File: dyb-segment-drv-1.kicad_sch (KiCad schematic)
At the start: 33 parts, among them J1 Conn_01x10, SW1 SW_SPDT, U1 AP2112K-1.8

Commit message: schem: add title
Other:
- company: (none) -> Rémi Ait-Younes
- title: (none) -> DYB Segment Driver 1
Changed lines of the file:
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@@
 	(generator_version "10.0")
 	(paper "A4")
+	(title_block
+		(title "DYB Segment Driver 1")
+		(date "2026-09-29")
+		(rev "01")
+		(company "Rémi Ait-Younes")
+	)
 	(rectangle
 		(start 15.24 168.91)

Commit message: schem: reannotate
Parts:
- renumbered C60 to C1, C61 to C2, JP4 to JP1, TP8 to TP1, TP27 to TP17, TP17 to TP18, TP18 to TP19, TP1 to TP2, TP19 to TP20, TP20 to TP21, TP21 to TP22, TP22 to TP23, TP23 to TP24, TP26 to TP25, TP2 to TP3, TP3 to TP4, TP4 to TP5, TP5 to TP6, TP6 to TP7, TP7 to TP8
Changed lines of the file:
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@@
 		(dnp no)
 		(fields_autoplaced yes)
-		(property "Reference" "#PWR0181"
+		(property "Reference" "#PWR07"
 			(at 80.01 191.77 0)
 			(hide yes)
@@
 			(project "dyb-segment-drv-1"
 				(path "/0d1f997b-7d97-47c3-85c1-1ce9346504d0"
-					(reference "#PWR0181")
+					(reference "#PWR07")
 					(unit 1)
 				)
@@
 		(in_pos_files yes)
 		(dnp no)
-		(property "Reference" "TP4"
+		(property "Reference" "TP5"
 			(at 128.778 76.2 0)
 			(show_name no)
@@
 			(project "dyb-segment-drv-1"
 				(path "/0d1f997b-7d97-47c3-85c1-1ce9346504d0"
-					(reference "TP4")
+					(reference "TP5")
 					(unit 1)
 				)
@@
 		(dnp no)
 		(fields_autoplaced yes)
-		(property "Reference" "#PWR0175"
+		(property "Reference" "#PWR03"
 			(at 39.37 198.12 0)
 			(hide yes)
@@
 			(project "dyb-segment-drv-1"
 				(path "/0d1f997b-7d97-47c3-85c1-1ce9346504d0"
-					(reference "#PWR0175")
+					(reference "#PWR03")
 					(unit 1)
 				)
@@
 		(in_pos_files yes)
 		(dnp no)
-		(property "Reference" "#PWR0173"
+		(property "Reference" "#PWR01"
 			(at 20.32 184.15 0)
 			(hide yes)
@@
 			(project "dyb-segment-drv-1"
 				(path "/0d1f997b-7d97-47c3-85c1-1ce9346504d0"
-					(reference "#PWR0173")
+					(reference "#PWR01")
 					(unit 1)
 				)
@@
 		(in_pos_files yes)
 		(dnp no)
-		(property "Reference" "TP6"
+		(property "Reference" "TP7"
 			(at 128.778 81.28 0)
 			(show_name no)
@@
 			(project "dyb-segment-drv-1"
 				(path "/0d1f997b-7d97-47c3-85c1-1ce9346504d0"
-					(reference "TP6")
+					(reference "TP7")
 					(unit 1)
 				)
@@
 		(in_pos_files yes)
 		(dnp no)
-		(property "Reference" "TP8"
+		(property "Reference" "TP1"
 			(at 46.228 175.768 0)
 			(show_name no)
@@
 			(project "dyb-segment-drv-1"
 				(path "/0d1f997b-7d97-47c3-85c1-1ce9346504d0"
-					(reference "TP8")
+					(reference "TP1")
 					(unit 1)
 				)
@@
 		(in_pos_files yes)
 		(dnp no)
-		(property "Reference" "TP23"
+		(property "Reference" "TP24"
 			(at 159.258 110.49 0)
 			(show_name no)
@@
 			(project "dyb-segment-drv-1"
 				(path "/0d1f997b-7d97-47c3-85c1-1ce9346504d0"
-					(reference "TP23")
+					(reference "TP24")
 					(unit 1)
 				)
@@
 		(dnp no)
 		(fields_autoplaced yes)
-		(property "Reference" "#PWR0176"
+		(property "Reference" "#PWR04"
 			(at 50.8 198.12 0)
 			(hide yes)
@@
 			(project "dyb-segment-drv-1"
 				(path "/0d1f997b-7d97-47c3-85c1-1ce9346504d0"
-					(reference "#PWR0176")
+					(reference "#PWR04")
 					(unit 1)
 				)
@@
 		(dnp no)
 		(fields_autoplaced yes)
-		(property "Reference" "#FLG02"
+		(property "Reference" "#FLG01"
 			(at 71.12 191.135 0)
 			(hide yes)
@@
 			(project "dyb-segment-drv-1"
 				(path "/0d1f997b-7d97-47c3-85c1-1ce9346504d0"
-					(reference "#FLG02")
+					(reference "#FLG01")
 					(unit 1)
 				)
@@
 		(in_pos_files yes)
 		(dnp no)
-		(property "Reference" "TP26"
+		(property "Reference" "TP25"
 			(at 159.258 113.03 0)
 			(show_name no)
@@
 			(project "dyb-segment-drv-1"
 				(path "/0d1f997b-7d97-47c3-85c1-1ce9346504d0"
-					(reference "TP26")
+					(reference "TP25")
 					(unit 1)
 				)
@@
 		(in_pos_files yes)
 		(dnp no)
-		(property "Reference" "TP7"
+		(property "Reference" "TP8"
 			(at 128.778 83.82 0)
 			(show_name no)
@@
 			(project "dyb-segment-drv-1"
 				(path "/0d1f997b-7d97-47c3-85c1-1ce9346504d0"
-					(reference "TP7")
+					(reference "TP8")
 					(unit 1)
 				)
@@
 		(dnp no)
 		(fields_autoplaced yes)
-		(property "Reference" "C61"
+		(property "Reference" "C2"
 			(at 54.61 185.4199 0)
 			(show_name no)
@@
 			(project "dyb-segment-drv-1"
 				(path "/0d1f997b-7d97-47c3-85c1-1ce9346504d0"
-					(reference "C61")
+					(reference "C2")
 					(unit 1)
 				)
@@
 		(dnp no)
 		(fields_autoplaced yes)
-		(property "Reference" "#PWR0178"
+		(property "Reference" "#PWR06"
 			(at 76.2 196.85 0)
 			(hide yes)
@@
 			(project "dyb-segment-drv-1"
 				(path "/0d1f997b-7d97-47c3-85c1-1ce9346504d0"
-					(reference "#PWR0178")
+					(reference "#PWR06")
 					(unit 1)
 				)
@@
 		(in_pos_files yes)
 		(dnp no)
-		(property "Reference" "#PWR0180"
+		(property "Reference" "#PWR09"
 			(at 123.19 100.33 0)
 			(hide yes)
@@
 			(project "dyb-segment-drv-1"
 				(path "/0d1f997b-7d97-47c3-85c1-1ce9346504d0"
-					(reference "#PWR0180")
+					(reference "#PWR09")
 					(unit 1)
 				)
@@
 		(in_pos_files yes)
 		(dnp no)
-		(property "Reference" "TP20"
+		(property "Reference" "TP21"
 			(at 159.258 102.87 0)
 			(show_name no)
@@
 			(project "dyb-segment-drv-1"
 				(path "/0d1f997b-7d97-47c3-85c1-1ce9346504d0"
-					(reference "TP20")
+					(reference "TP21")
 					(unit 1)
 				)
@@
 		(in_pos_files yes)
 		(dnp no)
-		(property "Reference" "#PWR0177"
+		(property "Reference" "#PWR05"
 			(at 53.34 184.15 0)
 			(hide yes)
@@
 			(project "dyb-segment-drv-1"
 				(path "/0d1f997b-7d97-47c3-85c1-1ce9346504d0"
-					(reference "#PWR0177")
+					(reference "#PWR05")
 					(unit 1)
 				)
@@
 		(in_pos_files yes)
 		(dnp no)
-		(property "Reference" "TP22"
+		(property "Reference" "TP23"
 			(at 159.258 107.95 0)
 			(show_name no)
@@
 			(project "dyb-segment-drv-1"
 				(path "/0d1f997b-7d97-47c3-85c1-1ce9346504d0"
-					(reference "TP22")
+					(reference "TP23")
 					(unit 1)
 				)
@@
 		(in_pos_files yes)
 		(dnp no)
-		(property "Reference" "TP27"
+		(property "Reference" "TP17"
 			(at 159.258 86.36 0)
 			(show_name no)
@@
 			(project "dyb-segment-drv-1"
 				(path "/0d1f997b-7d97-47c3-85c1-1ce9346504d0"
-					(reference "TP27")
+					(reference "TP17")
 					(unit 1)
 				)
@@
 		(in_pos_files yes)
 		(dnp no)
-		(property "Reference" "TP2"
+		(property "Reference" "TP3"
 			(at 128.778 71.12 0)
 			(show_name no)
@@
 			(project "dyb-segment-drv-1"
 				(path "/0d1f997b-7d97-47c3-85c1-1ce9346504d0"
-					(reference "TP2")
+					(reference "TP3")
 					(unit 1)
 				)
@@
 		(in_pos_files yes)
 		(dnp no)
-		(property "Reference" "TP18"
+		(property "Reference" "TP19"
 			(at 159.258 97.79 0)
 			(show_name no)
@@
 			(project "dyb-segment-drv-1"
 				(path "/0d1f997b-7d97-47c3-85c1-1ce9346504d0"
-					(reference "TP18")
+					(reference "TP19")
 					(unit 1)
 				)
@@
 		(in_pos_files yes)
 		(dnp no)
-		(property "Reference" "#PWR0179"
+		(property "Reference" "#PWR08"
 			(at 92.71 181.61 0)
 			(hide yes)
@@
 			(project "dyb-segment-drv-1"
 				(path "/0d1f997b-7d97-47c3-85c1-1ce9346504d0"
-					(reference "#PWR0179")
+					(reference "#PWR08")
 					(unit 1)
 				)
@@
 		(dnp no)
 		(fields_autoplaced yes)
-		(property "Reference" "#PWR0174"
+		(property "Reference" "#PWR02"
 			(at 22.86 198.12 0)
 			(hide yes)
@@
 			(project "dyb-segment-drv-1"
 				(path "/0d1f997b-7d97-47c3-85c1-1ce9346504d0"
-					(reference "#PWR0174")
+					(reference "#PWR02")
 					(unit 1)
 				)
@@
 		(in_pos_files yes)
 		(dnp no)
-		(property "Reference" "TP17"
+		(property "Reference" "TP18"
 			(at 159.258 95.25 0)
 			(show_name no)
@@
 			(project "dyb-segment-drv-1"
 				(path "/0d1f997b-7d97-47c3-85c1-1ce9346504d0"
-					(reference "TP17")
+					(reference "TP18")
 					(unit 1)
 				)
@@
 		(in_pos_files yes)
 		(dnp no)
-		(property "Reference" "TP3"
+		(property "Reference" "TP4"
 			(at 128.778 73.66 0)
 			(show_name no)
@@
 			(project "dyb-segment-drv-1"
 				(path "/0d1f997b-7d97-47c3-85c1-1ce9346504d0"
-					(reference "TP3")
+					(reference "TP4")
 					(unit 1)
 				)
@@
 		(dnp no)
 		(fields_autoplaced yes)
-		(property "Reference" "#FLG01"
+		(property "Reference" "#FLG02"
 			(at 92.71 183.515 0)
 			(hide yes)
@@
 			(project "dyb-segment-drv-1"
 				(path "/0d1f997b-7d97-47c3-85c1-1ce9346504d0"
-					(reference "#FLG01")
+					(reference "#FLG02")
 					(unit 1)
 				)
@@
 		(in_pos_files yes)
 		(dnp no)
-		(property "Reference" "TP5"
+		(property "Reference" "TP6"
 			(at 128.778 78.74 0)
 			(show_name no)
@@
 			(project "dyb-segment-drv-1"
 				(path "/0d1f997b-7d97-47c3-85c1-1ce9346504d0"
-					(reference "TP5")
+					(reference "TP6")
 					(unit 1)
 				)
@@
 		(in_pos_files yes)
 		(dnp no)
-		(property "Reference" "C60"
+		(property "Reference" "C1"
 			(at 20.066 185.42 0)
 			(show_name no)
@@
 			(project "dyb-segment-drv-1"
 				(path "/0d1f997b-7d97-47c3-85c1-1ce9346504d0"
-					(reference "C60")
+					(reference "C1")
 					(unit 1)
 				)
@@
 		(in_pos_files yes)
 		(dnp no)
-		(property "Reference" "JP4"
+		(property "Reference" "JP1"
 			(at 26.67 179.578 0)
 			(show_name no)
@@
 			(project "dyb-segment-drv-1"
 				(path "/0d1f997b-7d97-47c3-85c1-1ce9346504d0"
-					(reference "JP4")
+					(reference "JP1")
 					(unit 1)
 				)
@@
 		(in_pos_files yes)
 		(dnp no)
-		(property "Reference" "TP21"
+		(property "Reference" "TP22"
 			(at 159.258 105.41 0)
 			(show_name no)
@@
 			(project "dyb-segment-drv-1"
 				(path "/0d1f997b-7d97-47c3-85c1-1ce9346504d0"
-					(reference "TP21")
+					(reference "TP22")
 					(unit 1)
 				)
@@
 		(in_pos_files yes)
 		(dnp no)
-		(property "Reference" "TP1"
+		(property "Reference" "TP2"
 			(at 128.778 68.58 0)
 			(show_name no)
@@
 			(project "dyb-segment-drv-1"
 				(path "/0d1f997b-7d97-47c3-85c1-1ce9346504d0"
-					(reference "TP1")
+					(reference "TP2")
 					(unit 1)
 				)
@@
 		(in_pos_files yes)
 		(dnp no)
-		(property "Reference" "TP19"
+		(property "Reference" "TP20"
 			(at 159.258 100.33 0)
 			(show_name no)
@@
 			(project "dyb-segment-drv-1"
 				(path "/0d1f997b-7d97-47c3-85c1-1ce9346504d0"
-					(reference "TP19")
+					(reference "TP20")
 					(unit 1)
 				)

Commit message: schem: update power jmp footprint
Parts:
- JP1: footprint Connector_PinHeader_2.54mm:PinHeader_1x02_P2.54mm_Vertical -> Connector_PinHeader_2.54mm:PinHeader_1x02_P2.54mm_Horizontal
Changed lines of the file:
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@@
 			)
 		)
-		(property "Footprint" "Connector_PinHeader_2.54mm:PinHeader_1x02_P2.54mm_Vertical"
+		(property "Footprint" "Connector_PinHeader_2.54mm:PinHeader_1x02_P2.54mm_Horizontal"
 			(at 26.67 181.61 0)
 			(hide yes)

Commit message: pcb: add tooling holes and fiducials
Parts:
- added FID1, FID2, FID3: Fiducial, Fiducial:Fiducial_1mm_Mask2mm, symbol Mechanical:Fiducial
- added H1, H2, H3: MountingHole, MountingHole:ToolingHole_1.152mm, symbol Mechanical:MountingHole
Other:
- note added: "SMT assembly"

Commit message: pcb: add mounting holes
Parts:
- added H4, H5, H6: MountingHole_Pad, MountingHole:MountingHole_3.2mm_M3_Pad_Via, symbol Mechanical:MountingHole_Pad
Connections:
- net GND: now also H4.1, H5.1, H6.1
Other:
- note added: "Mounting"

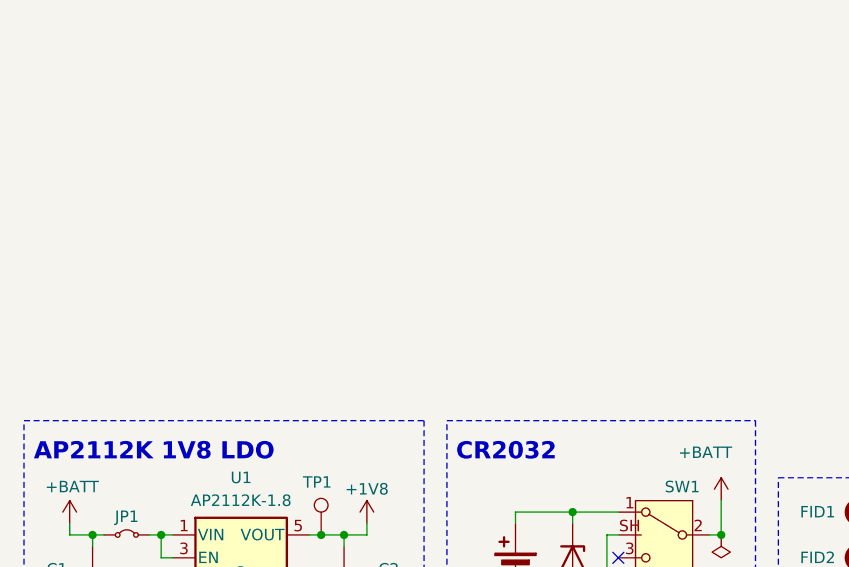
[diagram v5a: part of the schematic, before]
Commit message: schem: add input esd protection
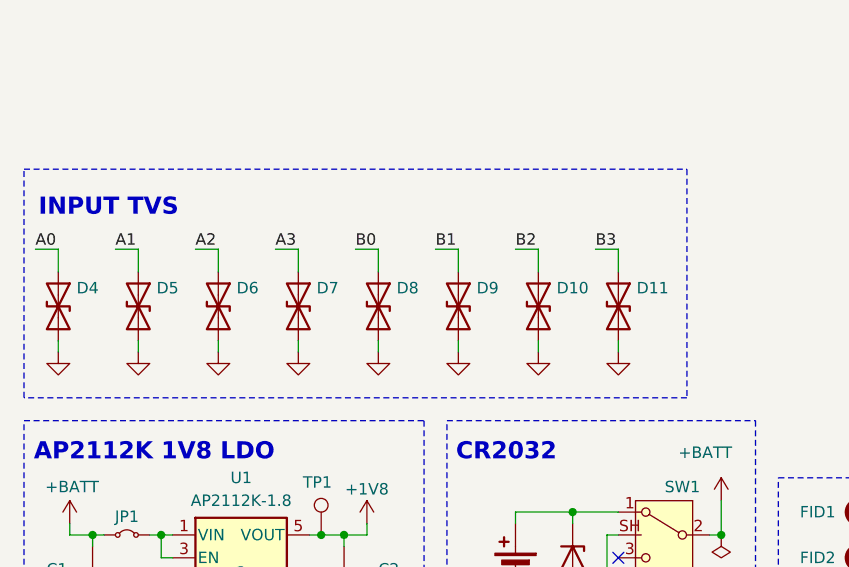
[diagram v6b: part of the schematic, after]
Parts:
- added D10, D11, D4, D5, D6, D7, D8, D9: H3V3L10B, GLCS:Diode_DFN1006, symbol Device:D_TVS
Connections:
- net A0: now also D4.1 (A1)
- net A1: now also D5.1 (A1)
- net A2: now also D6.1 (A1)
- net A3: now also D7.1 (A1)
- net B0: now also D8.1 (A1)
- net B1: now also D9.1 (A1)
- net B2: now also D10.1 (A1)
- net B3: now also D11.1 (A1)
- net GND: now also D10.2 (A2), D11.2 (A2), D4.2 (A2), D5.2 (A2), D6.2 (A2), D7.2 (A2), D8.2 (A2), D9.2 (A2)
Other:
- note added: "INPUT TVS"

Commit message: schem: update tvs part numbers
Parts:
- D10, D11, D4, D5, D6, D7, D8, D9: JLCPCB Part # C22395519 -> C20615781; Manufacturer Part Number H5VU10U -> H3V3L10B
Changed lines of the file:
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@@
 			)
 		)
-		(property "JLCPCB Part #" "C22395519"
+		(property "JLCPCB Part #" "C20615781"
 			(at 54.61 156.21 90)
 			(hide yes)
@@
 			)
 		)
-		(property "Manufacturer Part Number" "H5VU10U"
+		(property "Manufacturer Part Number" "H3V3L10B"
 			(at 54.61 156.21 90)
 			(hide yes)
@@
 			)
 		)
-		(property "JLCPCB Part #" "C22395519"
+		(property "JLCPCB Part #" "C20615781"
 			(at 27.94 156.21 90)
 			(hide yes)
@@
 			)
 		)
-		(property "Manufacturer Part Number" "H5VU10U"
+		(property "Manufacturer Part Number" "H3V3L10B"
 			(at 27.94 156.21 90)
 			(hide yes)
@@
 			)
 		)
-		(property "JLCPCB Part #" "C22395519"
+		(property "JLCPCB Part #" "C20615781"
 			(at 72.39 156.21 90)
 			(hide yes)
@@
 			)
 		)
-		(property "Manufacturer Part Number" "H5VU10U"
+		(property "Manufacturer Part Number" "H3V3L10B"
 			(at 72.39 156.21 90)
 			(hide yes)
@@
 			)
 		)
-		(property "JLCPCB Part #" "C22395519"
+		(property "JLCPCB Part #" "C20615781"
 			(at 63.5 156.21 90)
 			(hide yes)
@@
 			)
 		)
-		(property "Manufacturer Part Number" "H5VU10U"
+		(property "Manufacturer Part Number" "H3V3L10B"
 			(at 63.5 156.21 90)
 			(hide yes)
@@
 			)
 		)
-		(property "JLCPCB Part #" "C22395519"
+		(property "JLCPCB Part #" "C20615781"
 			(at 19.05 156.21 90)
 			(hide yes)
@@
 			)
 		)
-		(property "Manufacturer Part Number" "H5VU10U"
+		(property "Manufacturer Part Number" "H3V3L10B"
 			(at 19.05 156.21 90)
 			(hide yes)
@@
 			)
 		)
-		(property "JLCPCB Part #" "C22395519"
+		(property "JLCPCB Part #" "C20615781"
 			(at 45.72 156.21 90)
 			(hide yes)
@@
 			)
 		)
-		(property "Manufacturer Part Number" "H5VU10U"
+		(property "Manufacturer Part Number" "H3V3L10B"
 			(at 45.72 156.21 90)
 			(hide yes)
@@
 			)
 		)
-		(property "JLCPCB Part #" "C22395519"
+		(property "JLCPCB Part #" "C20615781"
 			(at 81.28 156.21 90)
 			(hide yes)
@@
 			)
 		)
-		(property "Manufacturer Part Number" "H5VU10U"
+		(property "Manufacturer Part Number" "H3V3L10B"
 			(at 81.28 156.21 90)
 			(hide yes)
@@
 			)
 		)
-		(property "JLCPCB Part #" "C22395519"
+		(property "JLCPCB Part #" "C20615781"
 			(at 36.83 156.21 90)
 			(hide yes)
@@
 			)
 		)
-		(property "Manufacturer Part Number" "H5VU10U"
+		(property "Manufacturer Part Number" "H3V3L10B"
 			(at 36.83 156.21 90)
 			(hide yes)

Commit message: schem: consolidate diode bom
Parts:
- removed D1: H5VU10U, GLCS:Diode_DFN1006, symbol GLCS:H5VU10U
- added D12: H3V3L10B, GLCS:Diode_DFN1006, symbol Device:D_TVS
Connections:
- net GND: now also D12.2 (A2)
- net at BT1.1 (+), SW1.1 (A): now also D12.1 (A1)
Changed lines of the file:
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@@
-	)
-	(symbol
-		(lib_id "GLCS:H5VU10U")
-		(at 76.2 184.15 270)
-		(unit 1)
-		(body_style 1)
-		(exclude_from_sim no)
-		(in_bom yes)
-		(on_board yes)
-		(in_pos_files yes)
-		(dnp no)
-		(property "Reference" "D1"
-			(at 71.374 187.452 90)
-			(show_name no)
-			(do_not_autoplace no)
-			(effects
-				(font
-					(size 1.27 1.27)
-				)
-				(justify left)
-			)
-		)
-		(property "Value" "H5VU10U"
-			(at 78.74 185.4199 90)
-			(hide yes)
-			(show_name no)
-			(do_not_autoplace no)
-			(effects
-				(font
-					(size 1.27 1.27)
-				)
-				(justify left)
-			)
-		)
-		(property "Footprint" "GLCS:Diode_DFN1006"
-			(at 71.755 184.15 0)
-			(hide yes)
-			(show_name no)
-			(do_not_autoplace no)
-			(effects
-				(font
-					(size 1.27 1.27)
-				)
-			)
-		)
-		(property "Datasheet" "https://datasheet.lcsc.com/lcsc/2504101957_hongjiacheng-H5VU10U_C22395519.pdf"
-			(at 76.2 184.15 0)
-			(hide yes)
-			(show_name no)
-			(do_not_autoplace no)
-			(effects
-				(font
-					(size 1.27 1.27)
-				)
-			)
-		)
-		(property "Description" "-55℃~+155℃ 0.8pF 16V 200nA 55W@8/20us 5A@8/20us 5V 6V ESD IEC 61000-4-2 Unidirectional DFN1006-2L ESD and Surge Protection (TVS/ESD) ROHS"
-			(at 76.2 184.15 0)
-			(hide yes)
-			(show_name no)
-			(do_not_autoplace no)
-			(effects
-				(font
-					(size 1.27 1.27)
-				)
-			)
-		)
-		(property "Basic" "E"
-			(at 76.2 184.15 90)
-			(hide yes)
-			(show_name no)
-			(do_not_autoplace no)
-			(effects
-				(font
-					(size 1.27 1.27)
-				)
-			)
-		)
-		(property "JLCPCB Part #" "C22395519"
-			(at 76.2 184.15 90)
-			(hide yes)
-			(show_name no)
-			(do_not_autoplace no)
-			(effects
-				(font
-					(size 1.27 1.27)
-				)
-			)
-		)
-		(property "Manufacturer" "hongjiacheng"
-			(at 76.2 184.15 90)
-			(hide yes)
-			(show_name no)
-			(do_not_autoplace no)
-			(effects
-				(font
-					(size 1.27 1.27)
-				)
-			)
-		)
-		(property "Manufacturer Part Number" "H5VU10U"
-			(at 76.2 184.15 90)
-			(hide yes)
-			(show_name no)
-			(do_not_autoplace no)
-			(effects
-				(font
-					(size 1.27 1.27)
-				)
-			)
-		)
-		(property "KLC_S3.3" ""
-			(at 76.2 184.15 90)
-			(hide yes)
-			(show_name no)
-			(do_not_autoplace no)
-			(effects
-				(font
-					(size 1.27 1.27)
-				)
-			)
-		)
-		(property "KLC_S4.1" ""
-			(at 76.2 184.15 90)
-			(hide yes)
-			(show_name no)
-			(do_not_autoplace no)
-			(effects
-				(font
-					(size 1.27 1.27)
-				)
-			)
-		)
-		(pin "1"
-		)
-		(pin "2"
-		)
-		(instances
-			(project "dyb-segment-drv-1"
-				(path "/0d1f997b-7d97-47c3-85c1-1ce9346504d0"
-					(reference "D1")
-					(unit 1)
-				)
-			)
-		)
 	)
 	(symbol
@@
 					(unit 1)
 				)
+			)
+		)
+	)
+	(symbol
+		(lib_id "Device:D_TVS")
+		(at 76.2 184.15 270)
+		(unit 1)
+		(body_style 1)
+		(exclude_from_sim no)
+		(in_bom yes)
+		(on_board yes)
+		(in_pos_files yes)
+		(dnp no)
+		(property "Reference" "D12"
+			(at 70.866 180.848 90)
+			(show_name no)
+			(do_not_autoplace no)
+			(effects
+				(font
+					(size 1.27 1.27)
+				)
+				(justify left)
+			)
+		)
+		(property "Value" "H3V3L10B"
+			(at 78.74 185.4199 90)
+			(hide yes)
+			(show_name no)
+			(do_not_autoplace no)
+			(effects
+				(font
+					(size 1.27 1.27)
+				)
+				(justify left)
+			)
+		)
+		(property "Footprint" "GLCS:Diode_DFN1006"
+			(at 76.2 184.15 0)
+			(hide yes)
+			(show_name no)
+			(do_not_autoplace no)
+			(effects
+				(font
+					(size 1.27 1.27)
+				)
+			)
+		)
+		(property "Datasheet" "https://datasheet.lcsc.com/lcsc/2504101957_hongjiacheng-H5VU10U_C22395519.pdf"
+			(at 76.2 184.15 0)
+			(hide yes)
+			(show_name no)
+			(do_not_autoplace no)
+			(effects
+				(font
+					(size 1.27 1.27)
+				)
+			)
+		)
+		(property "Description" "Bidirectional transient-voltage-suppression diode"
+			(at 76.2 184.15 0)
+			(hide yes)
+			(show_name no)
+			(do_not_autoplace no)
+			(effects
+				(font
+					(size 1.27 1.27)
+				)
+			)
+		)
+		(property "Basic" "E"
+			(at 76.2 184.15 90)
+			(hide yes)
+			(show_name no)
+			(do_not_autoplace no)
+			(effects
+				(font
+					(size 1.27 1.27)
+				)
+			)
+		)
+		(property "JLCPCB Part #" "C20615781"
+			(at 76.2 184.15 90)
+			(hide yes)
+			(show_name no)
+			(do_not_autoplace no)
+			(effects
+				(font
+					(size 1.27 1.27)
+				)
+			)
+		)
+		(property "Manufacturer" "hongjiacheng"
+			(at 76.2 184.15 90)
+			(hide yes)
+			(show_name no)
+			(do_not_autoplace no)
+			(effects
+				(font
+					(size 1.27 1.27)
+				)
+			)
+		)
+		(property "Manufacturer Part Number" "H3V3L10B"
+			(at 76.2 184.15 90)
+			(hide yes)
+			(show_name no)
+			(do_not_autoplace no)
+			(effects
+				(font
+					(size 1.27 1.27)
+				)
+			)
+		)
+		(pin "1"
+		)
+		(pin "2"
+		)
+		(instances
+			(project "dyb-segment-drv-1"
+				(path "/0d1f997b-7d97-47c3-85c1-1ce9346504d0"
+					(reference "D12")
+					(unit 1)
+				)
